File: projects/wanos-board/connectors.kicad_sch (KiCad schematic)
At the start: 9 parts, among them J14 12V_IN, J2 DOOR_SAUNA, J3 DOOR_BATH, J4 WATER_B1, J5 WATER_B2, J6 KWH_MAIN, J7 KWH_AUX, J8 BTN_SAUNA

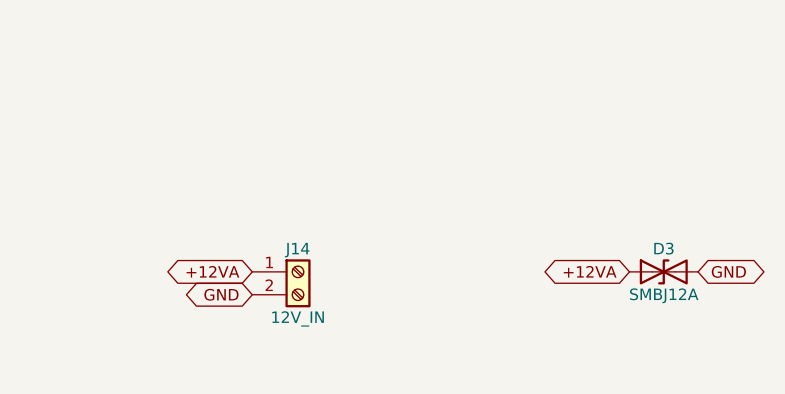
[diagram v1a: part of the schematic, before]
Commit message: SSR, power, IO_expander schemas update
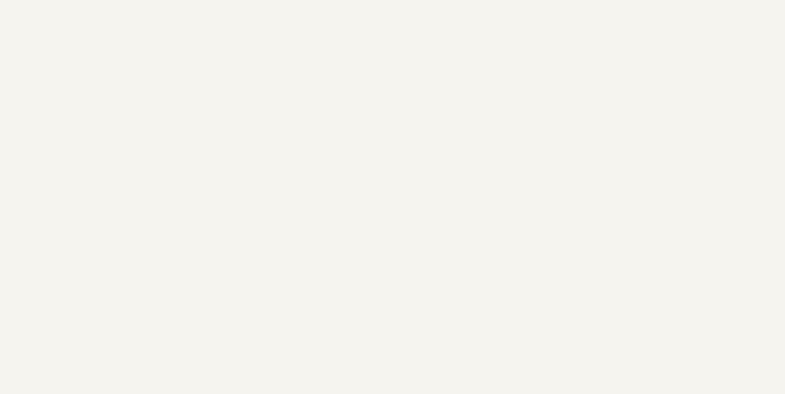
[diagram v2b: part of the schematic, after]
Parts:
- removed D3: SMBJ12A, Diode_SMD:D_SMB, symbol Device:D_TVS
- removed J14: 12V_IN, TerminalBlock_Phoenix:TerminalBlock_Phoenix_MKDS-1,5-2-5.08_1x02_P5.08mm_Horizontal, symbol Connector:Screw_Terminal_01x02

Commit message: 1st draft: water meters schematic
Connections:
- net GND: now also J4.5 (Pin_5), J5.5 (Pin_5)
- net +5VA: now reaches J5.4 (Pin_4)
- net +5VA: now also J4.4 (Pin_4), J4.6 (Pin_6), J5.6 (Pin_6)
- net EXP_A_P2_WM_B1_COLD renamed WM_B1_COLD
- net EXP_A_P3_WM_B1_HOT renamed WM_B1_HOT
- net EXP_A_P4_WM_B2_COLD renamed WM_B2_COLD
- net EXP_A_P5_WM_B2_HOT renamed WM_B2_HOT
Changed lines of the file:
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@@
 		)
 	)
-	(global_label "EXP_A_P4_WM_B2_COLD"
+	(global_label "WM_B2_COLD"
 		(shape bidirectional)
 		(at 25.4 127 180)
@@
 		)
 	)
-	(global_label "EXP_A_P3_WM_B1_HOT"
+	(global_label "WM_B1_HOT"
 		(shape bidirectional)
 		(at 25.4 90.17 180)
@@
 		)
 	)
-	(global_label "EXP_A_P2_WM_B1_COLD"
+	(global_label "WM_B1_COLD"
 		(shape bidirectional)
 		(at 25.4 87.63 180)
@@
 		)
 	)
-	(global_label "EXP_A_P5_WM_B2_HOT"
+	(global_label "WM_B2_HOT"
 		(shape bidirectional)
 		(at 25.4 129.54 180)
@@
 			(hide yes)
 			(show_name no)
+			(do_not_autoplace no)
+			(effects
+				(font
+					(size 1.27 1.27)
+				)
+			)
+		)
+	)
+	(global_label "+5VA"
+		(shape bidirectional)
+		(at 25.4 92.71 180)
+		(effects
+			(font
+				(size 1.27 1.27)
+			)
+			(justify right bottom)
+		)
+		(property "Intersheetrefs" "${INTERSHEET_REFS}"
+			(at 25.4 92.71 0)
+			(hide yes)
+			(show_name no)
+			(do_not_autoplace no)
+			(effects
+				(font
+					(size 1.27 1.27)
+				)
+			)
+		)
+	)
+	(global_label "GND"
+		(shape bidirectional)
+		(at 25.4 95.25 180)
+		(effects
+			(font
+				(size 1.27 1.27)
+			)
+			(justify right bottom)
+		)
+		(property "Intersheetrefs" "${INTERSHEET_REFS}"
+			(at 25.4 95.25 0)
+			(hide yes)
+			(show_name no)
+			(do_not_autoplace no)
+			(effects
+				(font
+					(size 1.27 1.27)
+				)
+			)
+		)
+	)
+	(global_label "+5VA"
+		(shape bidirectional)
+		(at 25.4 97.79 180)
+		(effects
+			(font
+				(size 1.27 1.27)
+			)
+			(justify right bottom)
+		)
+		(property "Intersheetrefs" "${INTERSHEET_REFS}"
+			(at 25.4 97.79 0)
+			(hide yes)
+			(show_name no)
+			(do_not_autoplace no)
+			(effects
+				(font
+					(size 1.27 1.27)
+				)
+			)
+		)
+	)
+	(global_label "+5VA"
+		(shape bidirectional)
+		(at 25.4 132.08 180)
+		(effects
+			(font
+				(size 1.27 1.27)
+			)
+			(justify right bottom)
+		)
+		(property "Intersheetrefs" "${INTERSHEET_REFS}"
+			(at 25.4 132.08 0)
+			(hide yes)
+			(show_name no)
+			(do_not_autoplace no)
+			(effects
+				(font
+					(size 1.27 1.27)
+				)
+			)
+		)
+	)
+	(global_label "GND"
+		(shape bidirectional)
+		(at 25.4 134.62 180)
+		(effects
+			(font
+				(size 1.27 1.27)
+			)
+			(justify right bottom)
+		)
+		(property "Intersheetrefs" "${INTERSHEET_REFS}"
+			(at 25.4 134.62 0)
+			(hide yes)
+			(show_name no)
+			(do_not_autoplace no)
+			(effects
+				(font
+					(size 1.27 1.27)
+				)
+			)
+		)
+	)
+	(global_label "+5VA"
+		(shape bidirectional)
+		(at 25.4 137.16 180)
+		(effects
+			(font
+				(size 1.27 1.27)
+			)
+			(justify right bottom)
+		)
+		(property "Intersheetrefs" "${INTERSHEET_REFS}"
+			(at 25.4 137.16 0)
+			(hide yes)
+			(show_name no)

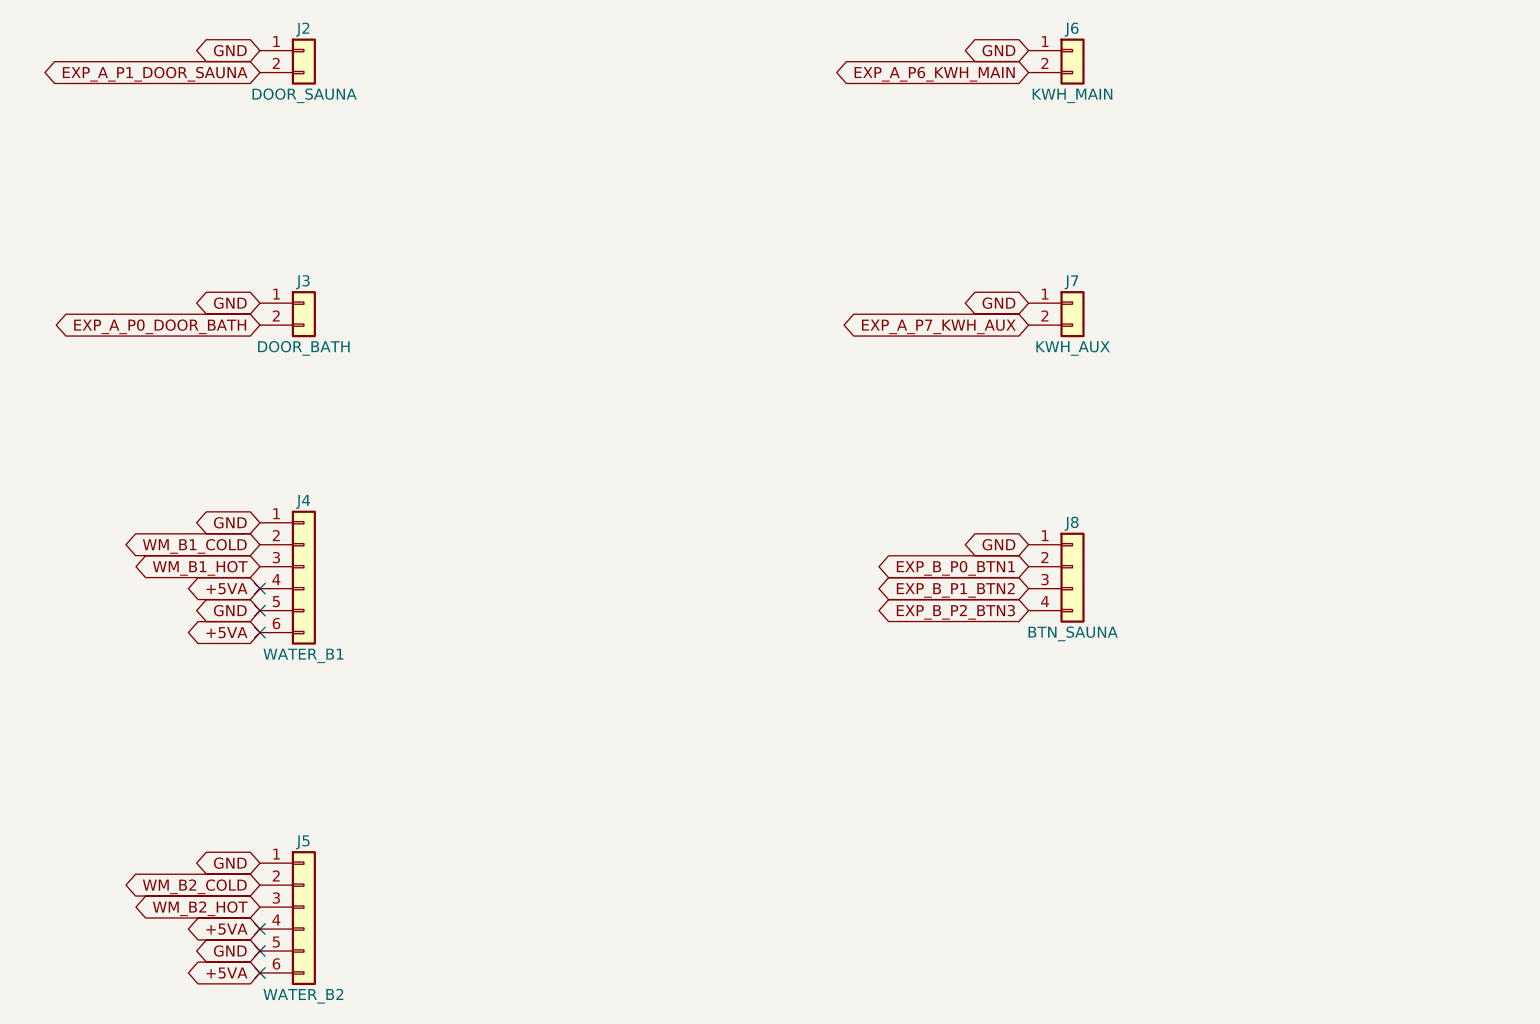
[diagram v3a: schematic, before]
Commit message: add RJ45 & TVS
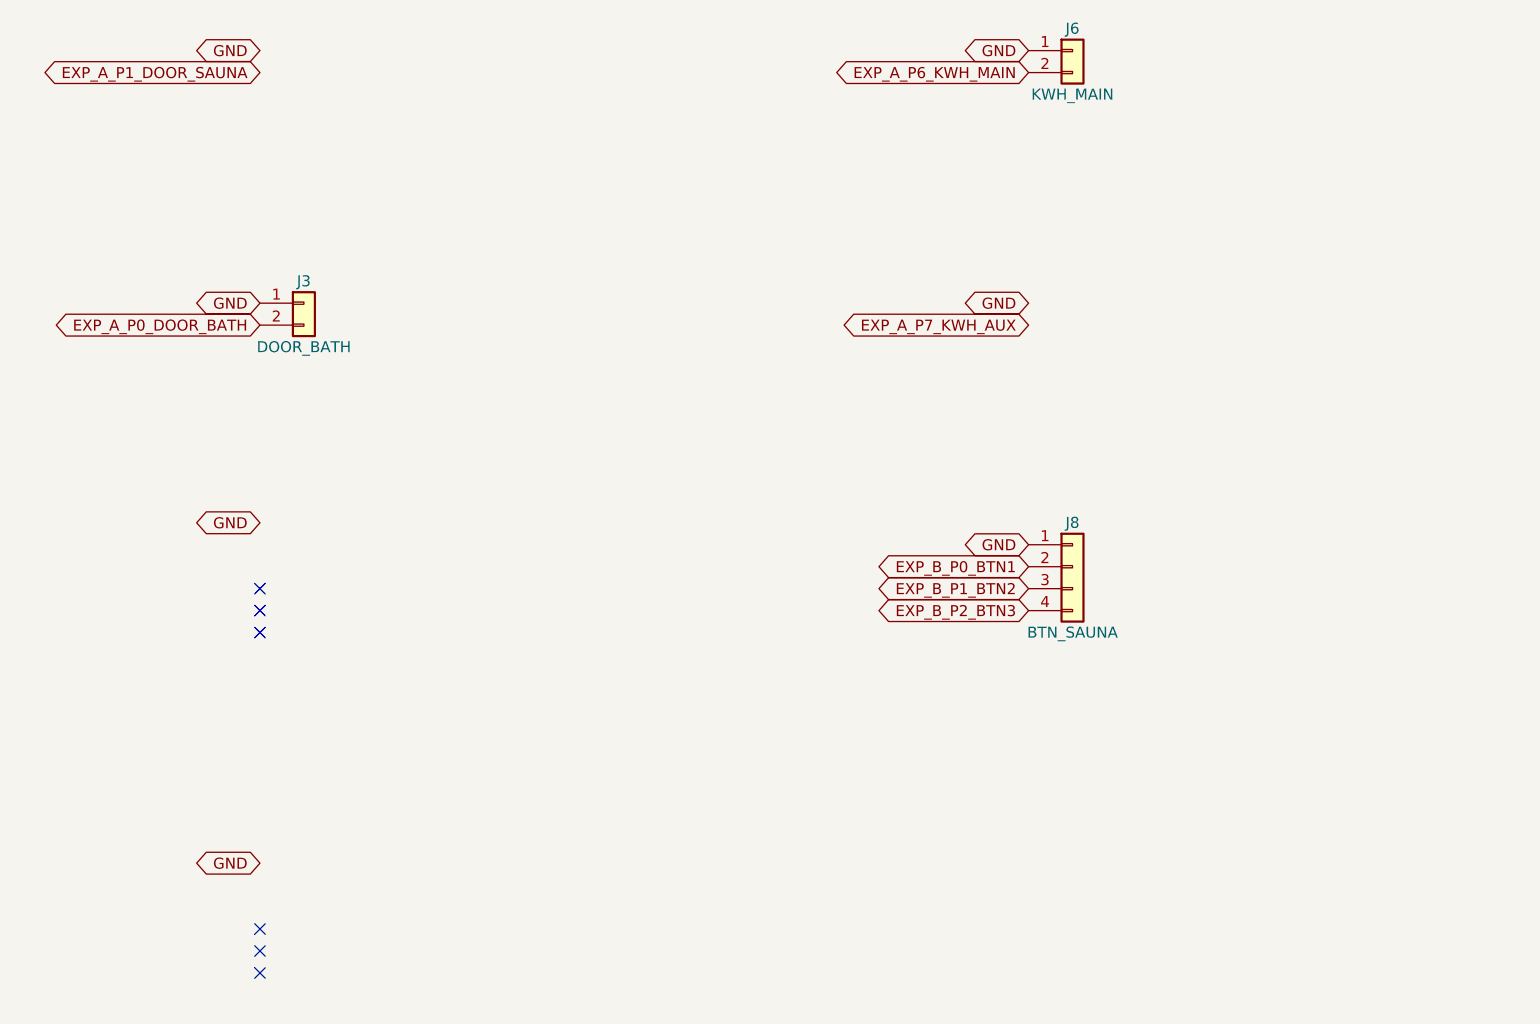
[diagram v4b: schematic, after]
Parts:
- removed J2: DOOR_SAUNA, Connector_JST:JST_XH_B2B-XH-A_1x02_P2.50mm_Vertical, symbol Connector_Generic:Conn_01x02
- removed J4: WATER_B1, Connector_JST:JST_XH_B6B-XH-A_1x06_P2.50mm_Vertical, symbol Connector_Generic:Conn_01x06
- removed J5: WATER_B2, Connector_JST:JST_XH_B6B-XH-A_1x06_P2.50mm_Vertical, symbol Connector_Generic:Conn_01x06
- removed J7: KWH_AUX, Connector_JST:JST_XH_B2B-XH-A_1x02_P2.50mm_Vertical, symbol Connector_Generic:Conn_01x02

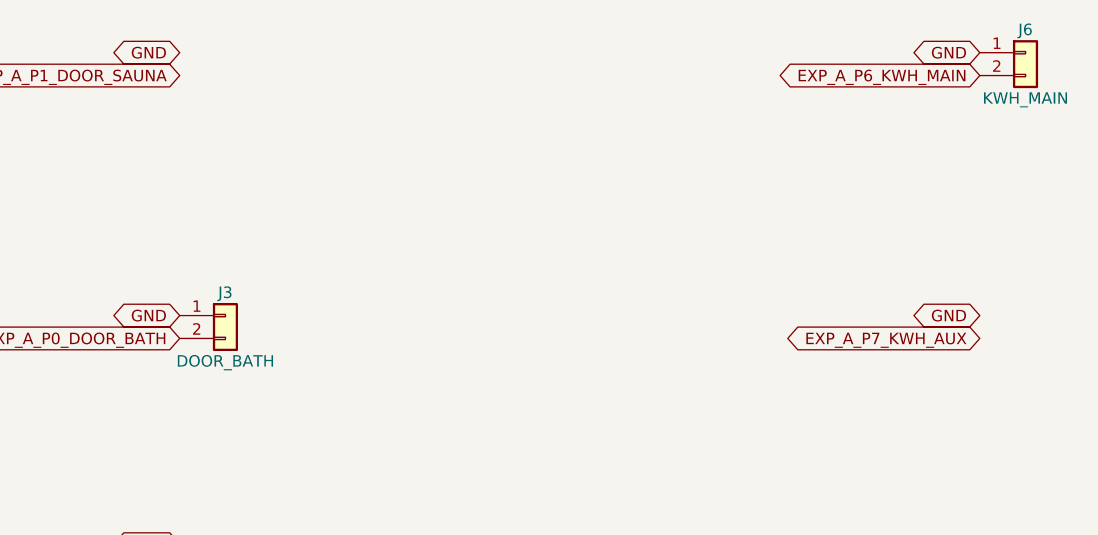
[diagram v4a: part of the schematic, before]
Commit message: watermeters schematic 2nd pass
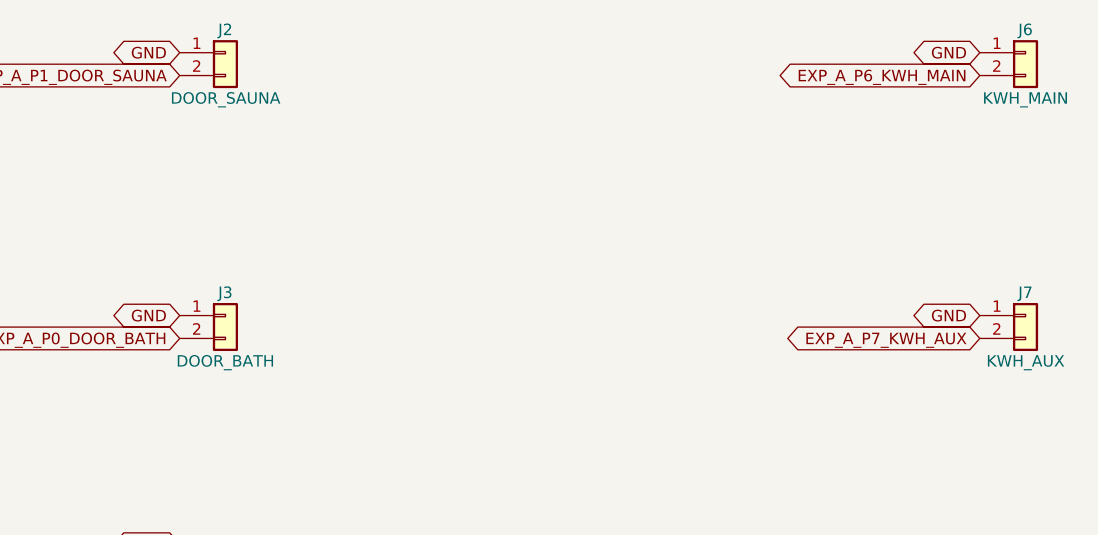
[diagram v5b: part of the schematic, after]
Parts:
- added J2: DOOR_SAUNA, Connector_JST:JST_XH_B2B-XH-A_1x02_P2.50mm_Vertical, symbol Connector_Generic:Conn_01x02
- added J7: KWH_AUX, Connector_JST:JST_XH_B2B-XH-A_1x02_P2.50mm_Vertical, symbol Connector_Generic:Conn_01x02
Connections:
- net EXP_A_P1_DOOR_SAUNA: now also J2.2 (Pin_2)
- net EXP_A_P7_KWH_AUX: now also J7.2 (Pin_2)
- net GND: now also J2.1 (Pin_1), J7.1 (Pin_1)
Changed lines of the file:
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@@
+		)
+	)
+	(symbol
+		(lib_id "Connector_Generic:Conn_01x02")
+		(at 30.48 30.48 0)
+		(unit 1)
+		(body_style 1)
+		(exclude_from_sim no)
+		(in_bom yes)
+		(on_board yes)
+		(in_pos_files yes)
+		(dnp no)
+		(property "Reference" "J2"
+			(at 30.48 27.94 0)
+			(show_name no)
+			(do_not_autoplace no)
+			(effects
+				(font
+					(size 1.27 1.27)
+				)
+			)
+		)
+		(property "Value" "DOOR_SAUNA"
+			(at 30.48 35.56 0)
+			(show_name no)
+			(do_not_autoplace no)
+			(effects
+				(font
+					(size 1.27 1.27)
+				)
+			)
+		)
+		(property "Footprint" "Connector_JST:JST_XH_B2B-XH-A_1x02_P2.50mm_Vertical"
+			(at 30.48 30.48 0)
+			(hide yes)
+			(show_name no)
+			(do_not_autoplace no)
+			(effects
+				(font
+					(size 1.27 1.27)
+				)
+			)
+		)
+		(property "Datasheet" ""
+			(at 30.48 30.48 0)
+			(hide yes)
+			(show_name no)
+			(do_not_autoplace no)
+			(effects
+				(font
+					(size 1.27 1.27)
+				)
+			)
+		)
+		(property "Description" "Generic connector, single row, 01x02, script generated (kicad-library-utils/schlib/autogen/connector/)"
+			(at 30.48 30.48 0)
+			(hide yes)
+			(show_name no)
+			(do_not_autoplace no)
+			(effects
+				(font
+					(size 1.27 1.27)
+				)
+			)
+		)
+		(pin "2"
+		)
+		(pin "1"
+		)
+		(instances
+			(project "connectors"
+				(path "/47dd188b-b977-4943-9943-e113444381d6"
+					(reference "J2")
+					(unit 1)
+				)
+			)
+			(project "wanos-board"
+				(path "/b64fe9be-4bba-4a4c-aa66-7fa6f4bbb662/08a79a1f-fed3-4b65-a041-bd4ae3cb853a"
+					(reference "J2")
+					(unit 1)
+				)
+			)
+		)
+	)
+	(symbol
+		(lib_id "Connector_Generic:Conn_01x02")
+		(at 119.38 59.69 0)
+		(unit 1)
+		(body_style 1)
+		(exclude_from_sim no)
+		(in_bom yes)
+		(on_board yes)
+		(in_pos_files yes)
+		(dnp no)
+		(property "Reference" "J7"
+			(at 119.38 57.15 0)
+			(show_name no)
+			(do_not_autoplace no)
+			(effects
+				(font
+					(size 1.27 1.27)
+				)
+			)
+		)
+		(property "Value" "KWH_AUX"
+			(at 119.38 64.77 0)
+			(show_name no)
+			(do_not_autoplace no)
+			(effects
+				(font
+					(size 1.27 1.27)
+				)
+			)
+		)
+		(property "Footprint" "Connector_JST:JST_XH_B2B-XH-A_1x02_P2.50mm_Vertical"
+			(at 119.38 59.69 0)
+			(hide yes)
+			(show_name no)
+			(do_not_autoplace no)
+			(effects
+				(font
+					(size 1.27 1.27)
+				)
+			)
+		)
+		(property "Datasheet" ""
+			(at 119.38 59.69 0)
+			(hide yes)
+			(show_name no)
+			(do_not_autoplace no)
+			(effects
+				(font
+					(size 1.27 1.27)
+				)
+			)
+		)
+		(property "Description" "Generic connector, single row, 01x02, script generated (kicad-library-utils/schlib/autogen/connector/)"
+			(at 119.38 59.69 0)
+			(hide yes)
+			(show_name no)
+			(do_not_autoplace no)
+			(effects
+				(font
+					(size 1.27 1.27)
+				)
+			)
+		)
+		(pin "1"
+		)
+		(pin "2"
+		)
+		(instances
+			(project "connectors"
+				(path "/47dd188b-b977-4943-9943-e113444381d6"
+					(reference "J7")
+					(unit 1)
+				)
+			)
+			(project "wanos-board"
+				(path "/b64fe9be-4bba-4a4c-aa66-7fa6f4bbb662/08a79a1f-fed3-4b65-a041-bd4ae3cb853a"
+					(reference "J7")
+					(unit 1)
+				)
+			)
 		)
 	)
